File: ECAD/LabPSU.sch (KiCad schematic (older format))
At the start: 55 parts, among them J1 PWR, U1 LM358

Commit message: Switch to digital control
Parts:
- removed D? (x2): 1N4148, symbol Device:D
- removed R?: 10K, symbol Device:R
- removed RV1: 300K, symbol Device:R_POT_Dual_Separate
- removed RV2: 250K, symbol Device:R_POT_Dual_Separate
- added C? (x2): 10uF, symbol Device:C
- added U?: LM1117-3.3, symbol Regulator_Linear:LM1117-3.3
- added U?: ATtiny1604-SS, Package_SO:SOIC-14_3.9x8.7mm_P1.27mm, symbol MCU_Microchip_ATtiny:ATtiny1604-SS
- added U?: MCP4812, symbol Analog_DAC:MCP4812
- R?: value 9.5K -> 70K
- R?: value 100K -> 10K
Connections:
- net labels added: +3.3V
- wire segments 165 -> 143
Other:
- note removed: "Rtop/Rbottom = Vout/1.23V - 1\nAdjustable 1.23V to 40V"
- moved on the sheet: R?, U1A, U1B, U1C

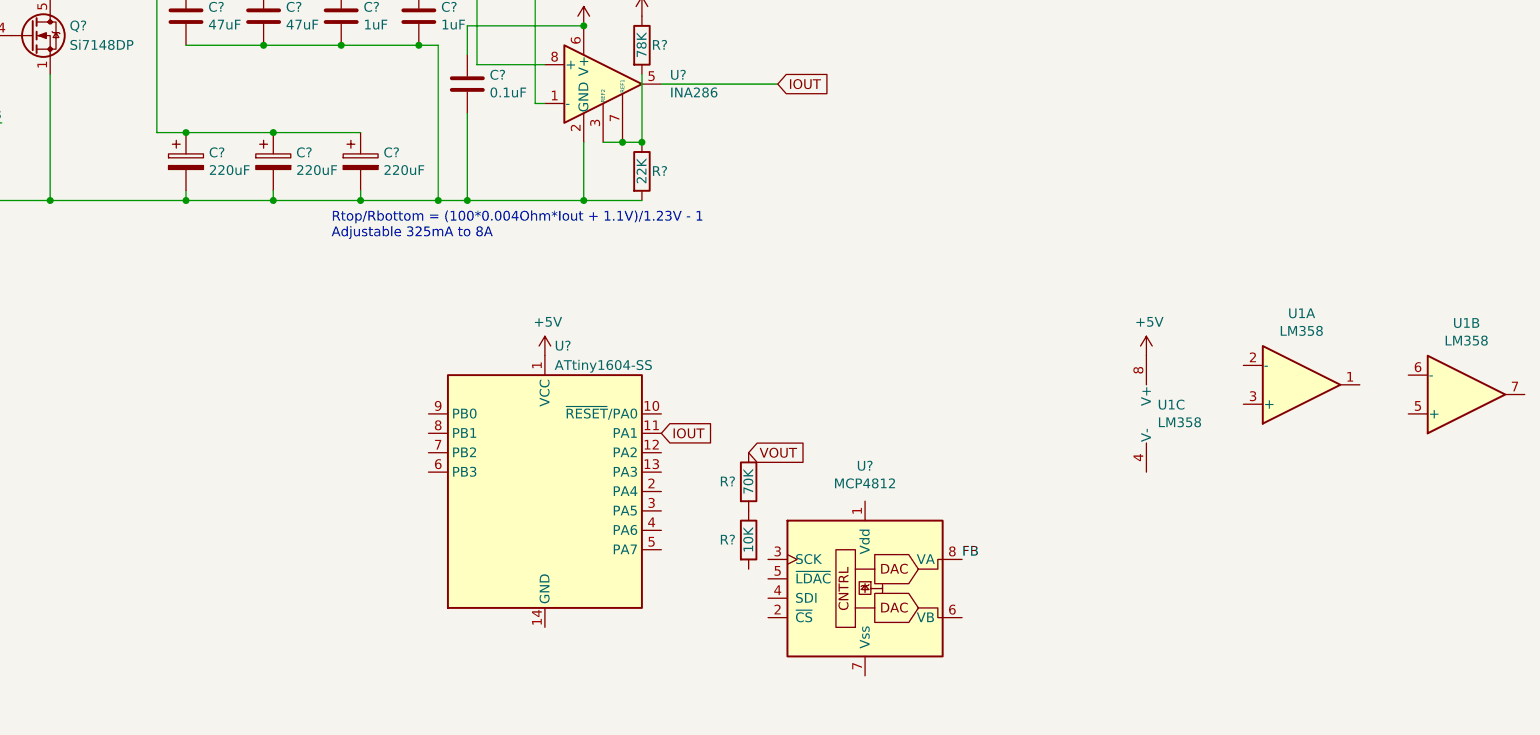
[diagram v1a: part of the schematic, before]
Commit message: Implement DAC
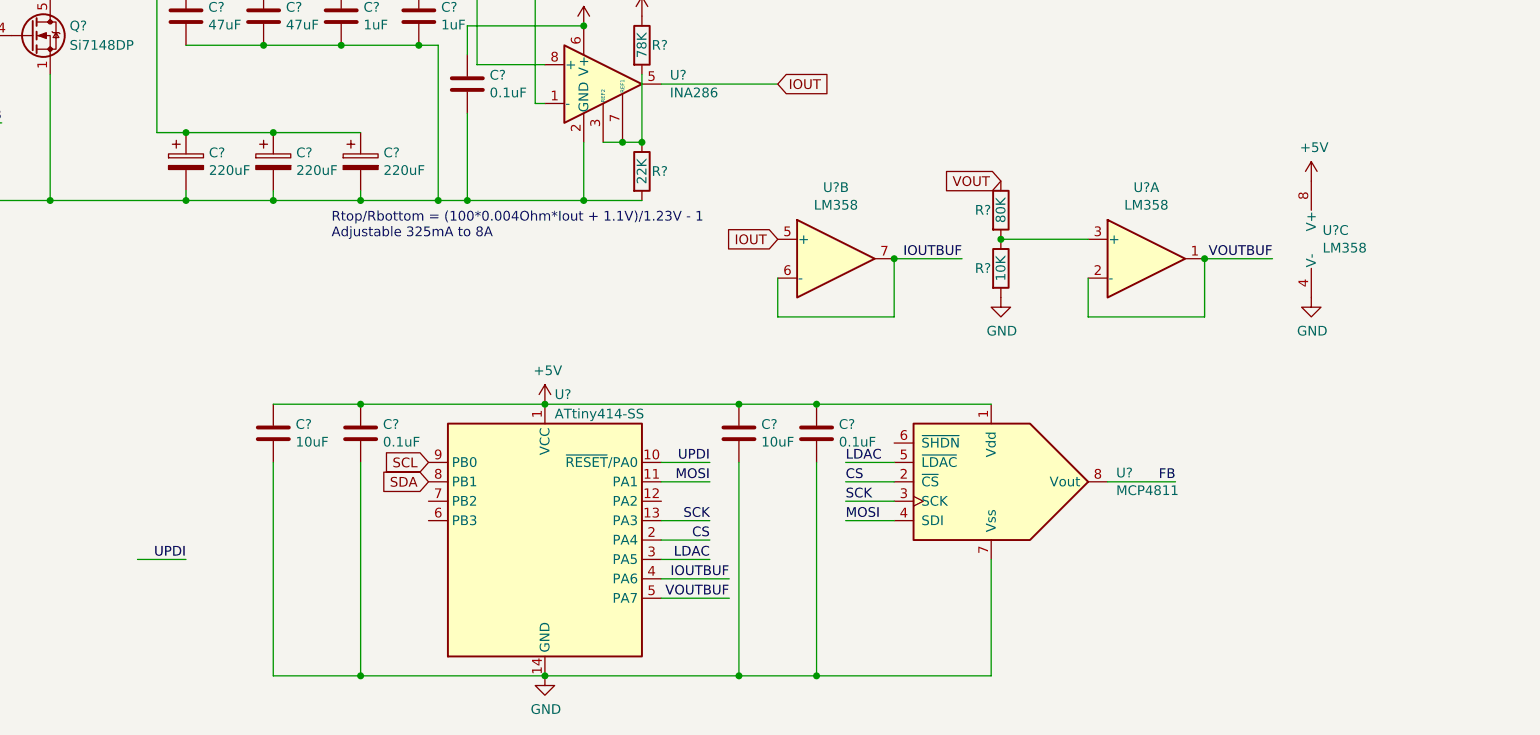
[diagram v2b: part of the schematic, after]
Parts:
- removed U1: LM358, symbol Amplifier_Operational:LM358
- removed U?: ATtiny1604-SS, Package_SO:SOIC-14_3.9x8.7mm_P1.27mm, symbol MCU_Microchip_ATtiny:ATtiny1604-SS
- removed U?: MCP4812, symbol Analog_DAC:MCP4812
- added C? (x2): 0.1uF, symbol Device:C
- added C? (x2): 10uF, symbol Device:C
- added U?: ATtiny414-SS, Package_SO:SOIC-14_3.9x8.7mm_P1.27mm, symbol MCU_Microchip_ATtiny:ATtiny414-SS
- added U? (x3): LM358, symbol Amplifier_Operational:LM358
- added U?: MCP4811, symbol Analog_DAC:MCP4811
- R?: value 70K -> 80K
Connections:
- net +5V: now also C?.1, C?.1, C?.1, C?.1, U?.1 (VCC), U?.1 (Vdd), U?.8 (V+)
- net FB: now also U?.8 (Vout)
- net GND: now also R?.2, C?.2, C?.2, C?.2, C?.2, U?.14 (GND), U?.4 (V-), U?.7 (Vss)
- net IOUT: now also U?.5 (+)
- net at R?.1, R?.2: now also U?.3 (+)
- new net CS: U?.2 (PA4), U?.2 (~CS)
- new net IOUTBUF: U?.4 (PA6), U?.6 (-), U?.7
- new net LDAC: U?.3 (PA5), U?.5 (~LDAC)
- new net MOSI: U?.11 (PA1), U?.4 (SDI)
- new net SCK: U?.13 (PA3), U?.3 (SCK)
- new net SCL: U?.9 (PB0)
- new net SDA: U?.8 (PB1)
- new net UPDI: U?.10 (~RESET~/PA0)
- new net VOUTBUF: U?.1, U?.2 (-), U?.5 (PA7)
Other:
- moved on the sheet: R?

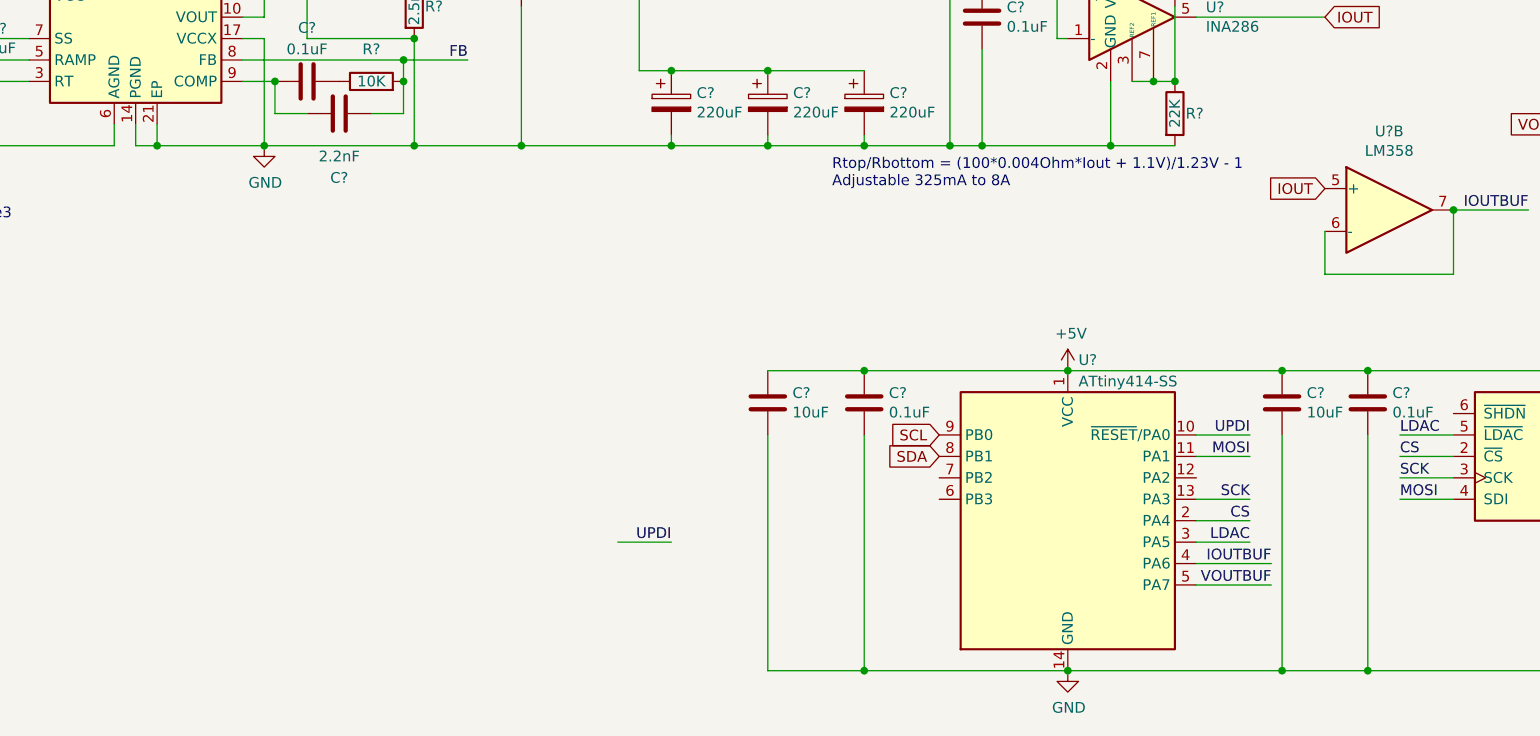
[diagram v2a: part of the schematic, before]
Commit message: Finish implementing digital scaler
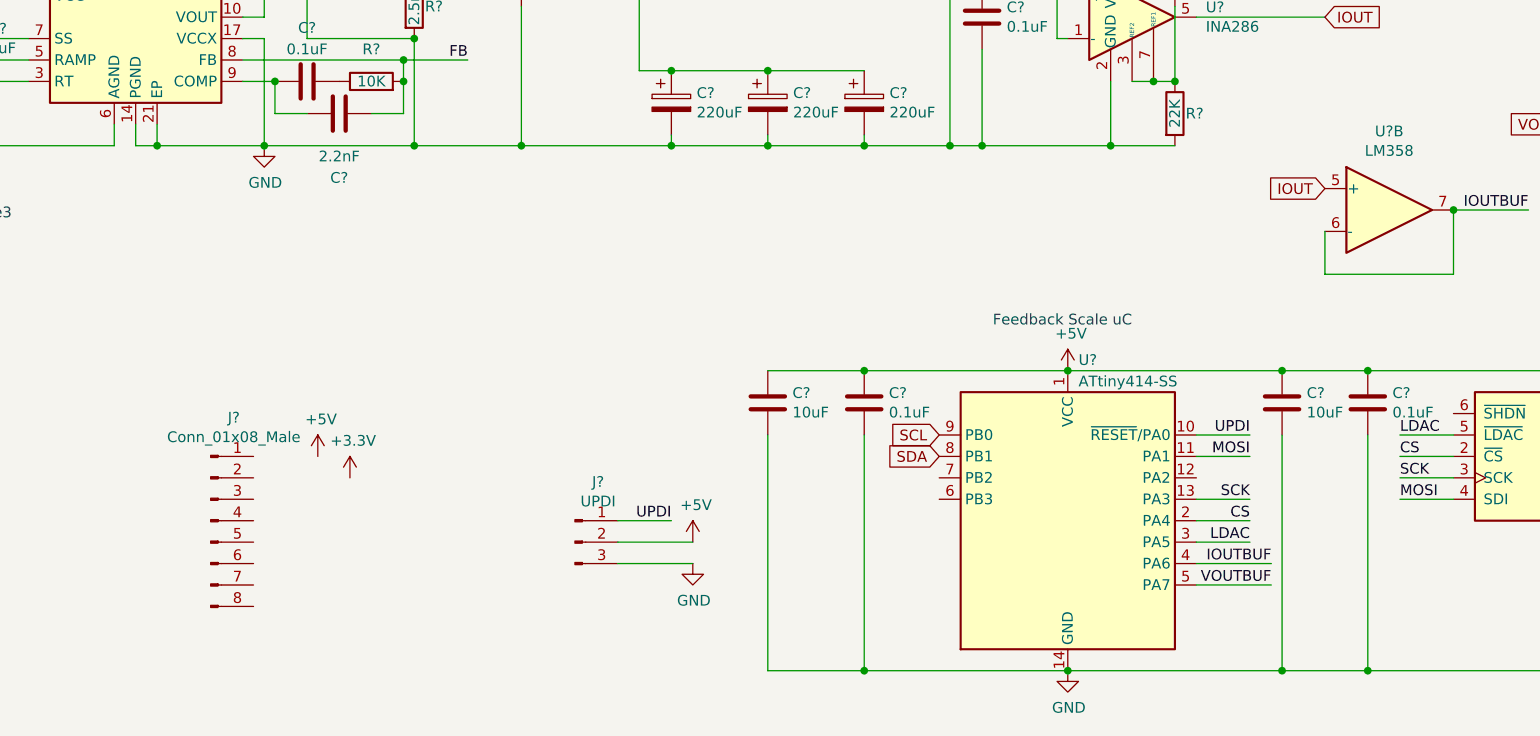
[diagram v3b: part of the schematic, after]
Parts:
- added J?: Conn_01x08_Male, symbol Connector:Conn_01x08_Male
- added J?: UPDI, symbol Connector:Conn_01x03_Male
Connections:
- net +5V: now also J?.2 (Pin_2)
- net GND: now also J?.3 (Pin_3)
- net UPDI: now also J?.1 (Pin_1)
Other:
- note added: "Feedback Scale uC"
- note removed: "Rtop/Rbottom = (100*0.004Ohm*Iout + 1.1V)/1.23V - 1\nAdjustable 325mA to 8A"
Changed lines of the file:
@@
 Text GLabel 2350 2400 2    50   Input ~ 0
 I_IN
-Text Notes 8150 4250 0    50   ~ 0
-Rtop/Rbottom = (100*0.004Ohm*Iout + 1.1V)/1.23V - 1\nAdjustable 325mA to 8A
 $Comp
 L Device:R R?
@@
 $EndComp
 Wire Wire Line
-	7150 5900 7400 5900
-Text Label 7400 5900 2    50   ~ 0
+	7150 5800 7400 5800
+Text Label 7400 5800 2    50   ~ 0
 UPDI
 Text GLabel 8650 5400 0    50   Input ~ 0
@@
 Text GLabel 8650 5500 0    50   Input ~ 0
 SDA
+$Comp
+L power:+5V #PWR?
+U 1 1 620460CA
+P 7500 5900
+F 0 "#PWR?" H 7500 5750 50  0001 C CNN
+F 1 "+5V" H 7515 6073 50  0000 C CNN
+F 2 "" H 7500 5900 50  0001 C CNN
+F 3 "" H 7500 5900 50  0001 C CNN
+	1    7500 5900
+	1    0    0    -1
+$EndComp
+$Comp
+L Connector:Conn_01x03_Male J?
+U 1 1 62058CB1
+P 6950 5900
+F 0 "J?" H 7058 6181 50  0000 C CNN
+F 1 "UPDI" H 7058 6090 50  0000 C CNN
+F 2 "" H 6950 5900 50  0001 C CNN
+F 3 "~" H 6950 5900 50  0001 C CNN
+	1    6950 5900
+	1    0    0    -1
+$EndComp
+$Comp
+L power:GND #PWR?
+U 1 1 62076809
+P 7500 6000
+F 0 "#PWR?" H 7500 5750 50  0001 C CNN
+F 1 "GND" H 7505 5827 50  0000 C CNN
+F 2 "" H 7500 6000 50  0001 C CNN
+F 3 "" H 7500 6000 50  0001 C CNN
+	1    7500 6000
+	1    0    0    -1
+$EndComp
+Wire Wire Line
+	7150 5900 7500 5900
+Wire Wire Line
+	7150 6000 7500 6000
+$Comp
+L Connector:Conn_01x08_Male J?
+U 1 1 62046D76
+P 5250 5800
+F 0 "J?" H 5358 6281 50  0000 C CNN
+F 1 "Conn_01x08_Male" H 5358 6190 50  0000 C CNN
+F 2 "" H 5250 5800 50  0001 C CNN
+F 3 "~" H 5250 5800 50  0001 C CNN
+	1    5250 5800
+	1    0    0    -1
+$EndComp
+$Comp
+L power:+5V #PWR?
+U 1 1 62048CB3
+P 5750 5500
+F 0 "#PWR?" H 5750 5350 50  0001 C CNN
+F 1 "+5V" H 5765 5673 50  0000 C CNN
+F 2 "" H 5750 5500 50  0001 C CNN
+F 3 "" H 5750 5500 50  0001 C CNN
+	1    5750 5500
+	1    0    0    -1
+$EndComp
+$Comp
+L power:+3.3V #PWR?
+U 1 1 62052B66
+P 5900 5600
+F 0 "#PWR?" H 5900 5450 50  0001 C CNN
+F 1 "+3.3V" H 5915 5773 50  0000 C CNN
+F 2 "" H 5900 5600 50  0001 C CNN
+F 3 "" H 5900 5600 50  0001 C CNN
+	1    5900 5600
+	1    0    0    -1
+$EndComp
+Text Notes 8900 4900 0    50   ~ 0
+Feedback Scale uC
 $EndSCHEMATC

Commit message: rework a few things
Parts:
- removed J?: Conn_01x08_Male, symbol Connector:Conn_01x08_Male
- removed R?: 22K, symbol Device:R
- removed R?: 78K, symbol Device:R
- added U?: MCP4812, symbol Analog_DAC:MCP4812
- R?: value 9K -> 90K
- R?: value 1K -> 10K
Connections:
- net +3V3: now also C?.1, C?.1, C?.1, C?.1, C?.1, C?.1, J?.2 (Pin_2), U?.1 (VCC), U?.1 (Vdd), U?.5 (V+), U?.6 (V+), U?.8 (V+), U?.8 (V+)
- net +5V: no longer C?.1, C?.1, C?.1, C?.1, C?.1, C?.1, J?.2 (Pin_2), U?.1 (VCC), U?.1 (Vdd), U?.5 (V+), U?.6 (V+), U?.8 (V+)
- net GND: now also U?.3 (REF2), U?.7 (REF1)
- net VBUS: now also R?.1; no longer U?.3 (+), U?.8 (V+)
- net VSET: now also U?.2 (-); no longer U?.5 (+)
- net at R?.1, R?.2: now also U?.3 (+), U?.5 (+); no longer U?.6 (-)
- new net: U?.6 (-), U?.7
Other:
- moved on the sheet: R?, U?B, U?C

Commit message: external adc
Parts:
- added C? (x2): 0.1uF, symbol Device:C
- added C? (x2): 10uF, symbol Device:C
- added R?: 3.7K, symbol Device:R
- added R?: 10K, symbol Device:R
- added TP?: VIN, symbol Connector:TestPoint
- added TP?: IIN, symbol Connector:TestPoint
- added TP?: 5V, symbol Connector:TestPoint
- added TP?: 3V3, symbol Connector:TestPoint
- added TP?: EN, symbol Connector:TestPoint
- added TP?: SET, symbol Connector:TestPoint
- added TP?: OUT, symbol Connector:TestPoint
- added TP?: FB, symbol Connector:TestPoint
- added TP?: IOUT, symbol Connector:TestPoint
- added TP?: BUCKSW, symbol Connector:TestPoint
- added TP?: BOOSTSW, symbol Connector:TestPoint
- added TP? (x2): GND, symbol Connector:TestPoint
- added U?: MCP3204, symbol Analog_ADC:MCP3204
- R?: value 90K -> 150K
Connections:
- net +3V3: now also TP?.1; no longer C?.1, C?.1, C?.1, C?.1, C?.1, U?.1 (VCC), U?.1 (Vdd), U?.6 (V+), U?.8 (V+)
- net +5V: now also C?.1, C?.1, C?.1, C?.1, C?.1, U?.1 (VCC), U?.1 (Vdd), U?.1 (Vdd), U?.6 (V+), U?.8 (V+), C?.1, C?.1, C?.1, C?.1, TP?.1, U?.13 (Vref), U?.14 (Vdd)
- net EN: now also TP?.1
- net FB: now also TP?.1
- net GND: now also U?.7 (Vss), C?.2, C?.2, C?.2, C?.2, R?.1, TP?.1, TP?.1, U?.12 (AGND), U?.5 (NC), U?.6 (NC), U?.7 (DGND)
- net IOUT: now also TP?.1
- net IOUTBUF: now also R?.2, U?.2 (CH1); no longer U?.4 (PA6), U?.6 (-)
- net I_IN: now also TP?.1
- net MOSI: now also U?.9 (Din)
- net SCK: now also U?.11 (CLK)
- net VBUS: now also TP?.1
- net VOUTBUF: now also U?.1 (CH0); no longer U?.5 (PA7)
- net VSET: now also TP?.1
- net at C?.2, D?.1 (K), L?.1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: now also TP?.1
- net at D?.2 (A), L?.2, Q?.5 (D): now also TP?.1
- net at C?.1, C?.1, C?.1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: now also TP?.1
- net MISO: now reaches U?.12 (PA2)
- net MISO: now also U?.10 (Dout)
- net VIN_BUF: now reaches U?.6 (-), U?.7
- net IOUTSET: now reaches U?.6 (VB)
- net IOUTSET: now also U?.4 (CH3)
- net VOUTSET: now reaches U?.8 (VA)
- net VOUTSET: now also U?.3 (CH2)
- net CS renamed CS0
- net SCL: no longer names the net of U?.9 (PB0)
- net SDA: no longer names the net of U?.8 (PB1)
- new net: R?.1, R?.2, U?.6 (-)
- new net CS1: U?.4 (PA6), U?.8 (~CS~/SHDN)
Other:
- moved on the sheet: R?, U?, U?A, U?B, U?C
